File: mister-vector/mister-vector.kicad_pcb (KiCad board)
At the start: 4 copper layers, 68.6 x 106.6 mm, 132 parts, among them IC1 SN74ALVCH16841DL, IC2 74HC32D, IC3 74HC139D, IC4 SN74ALVCH16841DL, IC5 TL084, IC6 SN74ALVCH16841DL, IC7 TL084, J2 AUDIO_JACK_3.5MM_KIT, U1 VASD1-SIP

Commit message: relink refdegs
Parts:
- GPIO1: value (none) -> PINHD-2X20
- IC2: value 74HC32D -> 7432D
- IC3: value 74HC139D -> 74139D
- J1, J3: value (none) -> 618015330923
- JP1: value (none) -> JP2E
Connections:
- net +12V_OPAMP renamed /+12V_OPAMP
- net +VREF renamed /+VREF
- net -12V_OPAMP renamed /-12V_OPAMP
- net AUDIO_L renamed /AUDIO_L
- net AUDIO_R renamed /AUDIO_R
- net B+ renamed /B+
- net B1+ renamed Net-(IC5C-OUT)
- net BTN_OSD renamed /BTN_OSD
- net BTN_RESET renamed /BTN_RESET
- net BTN_USER renamed /BTN_USER
- net DAC1_B0 renamed /DAC1_B0
- net DAC1_B1 renamed /DAC1_B1
- net DAC1_B2 renamed /DAC1_B2
- net DAC1_B3 renamed /DAC1_B3
- net DAC1_B4 renamed /DAC1_B4
- net DAC1_B5 renamed /DAC1_B5
- net DAC1_G0 renamed /DAC1_G0
- net DAC1_G1 renamed /DAC1_G1
- net DAC1_G2 renamed /DAC1_G2
- net DAC1_G3 renamed /DAC1_G3
- net DAC1_G4 renamed /DAC1_G4
- net DAC1_G5 renamed /DAC1_G5
- net DAC1_HSYNC renamed /DAC1_HSYNC
- net DAC1_LAT renamed /DAC1_LAT
- net DAC1_R0 renamed /DAC1_R0
- net DAC1_R1 renamed /DAC1_R1
- net DAC1_R2 renamed /DAC1_R2
- net DAC1_R3 renamed /DAC1_R3
- net DAC1_R4 renamed /DAC1_R4
- net DAC1_R5 renamed /DAC1_R5
- net DAC1_VSYNC renamed /DAC1_VSYNC
- net DAC2_B0 renamed /DAC2_B0
- net DAC2_B1 renamed /DAC2_B1
- net DAC2_B2 renamed /DAC2_B2
- net DAC2_B3 renamed /DAC2_B3
- net DAC2_B4 renamed /DAC2_B4
- net DAC2_B5 renamed /DAC2_B5
- net DAC2_G0 renamed /DAC2_G0
- net DAC2_G1 renamed /DAC2_G1
- net DAC2_G2 renamed /DAC2_G2
- net DAC2_G3 renamed /DAC2_G3
- net DAC2_G4 renamed /DAC2_G4
- net DAC2_G5 renamed /DAC2_G5
- net DAC2_HSYNC renamed /DAC2_HSYNC
- net DAC2_LAT renamed /DAC2_LAT
- net DAC2_R0 renamed /DAC2_R0
- net DAC2_R1 renamed /DAC2_R1
- net DAC2_R2 renamed /DAC2_R2
- net DAC2_R3 renamed /DAC2_R3
- net DAC2_R4 renamed /DAC2_R4
- net DAC2_R5 renamed /DAC2_R5
- net DAC2_VSYNC renamed /DAC2_VSYNC
- net DAC3_LAT renamed /DAC3_LAT
- net DAC4_LAT renamed /DAC4_LAT
- net DAC_X renamed /DAC_X
- net DAC_Y renamed /DAC_Y
- net G+ renamed /G+
- net G1+ renamed Net-(IC5A-OUT)
- net HSYNC renamed /HSYNC
- net I1+ renamed Net-(IC5D-OUT)
- net LATCH_EN_N renamed /LATCH_EN_N
- net LED_DISK renamed /LED_DISK
- net LED_POWER renamed /LED_POWER
- net LED_USER renamed /LED_USER
- net R+ renamed /R+
- net R1+ renamed Net-(IC5B-OUT)
- net SD_CLK renamed /SD_CLK
- net SD_CMD renamed /SD_CMD
- net SD_DAT0 renamed /SD_DAT0
- net SD_DAT1 renamed /SD_DAT1
- net SD_DAT2 renamed /SD_DAT2
- net SD_DAT3 renamed /SD_DAT3
- net SPDIF renamed /SPDIF
- net VEC_X+ renamed /VEC_X+
- net VEC_X0 renamed /VEC_X0
- net VEC_X1 renamed /VEC_X1
- net VEC_X2 renamed /VEC_X2
- net VEC_X3 renamed /VEC_X3
- net VEC_X4 renamed /VEC_X4
- net VEC_X5 renamed /VEC_X5
- net VEC_X6 renamed /VEC_X6
- net VEC_X7 renamed /VEC_X7
- net VEC_X8 renamed /VEC_X8
- net VEC_X9 renamed /VEC_X9
- net VEC_Y+ renamed /VEC_Y+
- net VEC_Y0 renamed /VEC_Y0
- net VEC_Y1 renamed /VEC_Y1
- net VEC_Y2 renamed /VEC_Y2
- net VEC_Y3 renamed /VEC_Y3
- net VEC_Y4 renamed /VEC_Y4
- net VEC_Y5 renamed /VEC_Y5
- net VEC_Y6 renamed /VEC_Y6
- net VEC_Y7 renamed /VEC_Y7
- net VEC_Y8 renamed /VEC_Y8
- net VEC_Y9 renamed /VEC_Y9
- net VGA1_B renamed /VGA1_B
- net VGA1_G renamed /VGA1_G
- net VGA1_HSYNC renamed /VGA1_HSYNC
- net VGA1_R renamed /VGA1_R
- net VGA1_VSYNC renamed /VGA1_VSYNC
- net VGA2_B renamed /VGA2_B
- net VGA2_G renamed /VGA2_G
- net VGA2_HSYNC renamed /VGA2_HSYNC
- net VGA2_R renamed /VGA2_R
- net VGA2_VSYNC renamed /VGA2_VSYNC
- net VGA_B0 renamed /VGA_B0
- net VGA_B1 renamed /VGA_B1
- net VGA_B2 renamed /VGA_B2
- net VGA_B3 renamed /VGA_B3
- net VGA_B4 renamed /VGA_B4
- net VGA_B5 renamed /VGA_B5
- net VGA_G0 renamed /VGA_G0
- net VGA_G1 renamed /VGA_G1
- net VGA_G2 renamed /VGA_G2
- net VGA_G3 renamed /VGA_G3
- net VGA_G4 renamed /VGA_G4
- net VGA_G5 renamed /VGA_G5
- net VGA_R0 renamed /VGA_R0
- net VGA_R1 renamed /VGA_R1
- net VGA_R2 renamed /VGA_R2
- net VGA_R3 renamed /VGA_R3
- net VGA_R4 renamed /VGA_R4
- net VGA_R5 renamed /VGA_R5
- net VSYNC renamed /VSYNC
- IC3 pad 11: (no net) -> unconnected-(IC3B-Y1-Pad11)
- IC3 pad 12: (no net) -> unconnected-(IC3B-Y0-Pad12)
- IC3 pad 9: (no net) -> unconnected-(IC3B-Y3-Pad9)
- J1 pad 11: (no net) -> unconnected-(J1-Pad11)
- J1 pad 12: (no net) -> unconnected-(J1-Pad12)
- J1 pad 15: (no net) -> unconnected-(J1-Pad15)
- J1 pad 4: (no net) -> unconnected-(J1-Pad4)
- J1 pad 9: (no net) -> unconnected-(J1-Pad9)
- J1 pad SHELL: (no net) -> Net-(J1-SHIELD-PadSHELL)
- J1 pad SHELL1: (no net) -> Net-(J1-SHIELD-PadSHELL)
- J2 pad RSH: (no net) -> unconnected-(J2-PadRSH)
- J2 pad TSH: (no net) -> unconnected-(J2-PadTSH)
- J3 pad 11: (no net) -> unconnected-(J3-Pad11)
- J3 pad 12: (no net) -> unconnected-(J3-Pad12)
- J3 pad 15: (no net) -> unconnected-(J3-Pad15)
- J3 pad 4: (no net) -> unconnected-(J3-Pad4)
- J3 pad 9: (no net) -> unconnected-(J3-Pad9)
- J3 pad SHELL: (no net) -> Net-(J3-SHIELD-PadSHELL)
- J3 pad SHELL1: (no net) -> Net-(J3-SHIELD-PadSHELL)
- X_SIZE0 pad A: (no net) -> unconnected-(X_SIZE0-PadA)
- Y_SIZE0 pad A: (no net) -> unconnected-(Y_SIZE0-PadA)
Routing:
- added copper zone on B.Cu, net (none)
- added copper zone on F.Cu, net (none)
- added copper zone on In1.Cu, net (none)
- added copper zone on In2.Cu, net (none)
- removed copper zone on B.Cu, net GND
- removed copper zone on F.Cu, net GND
- removed copper zone on In1.Cu, net GND
- removed copper zone on In2.Cu, net GND

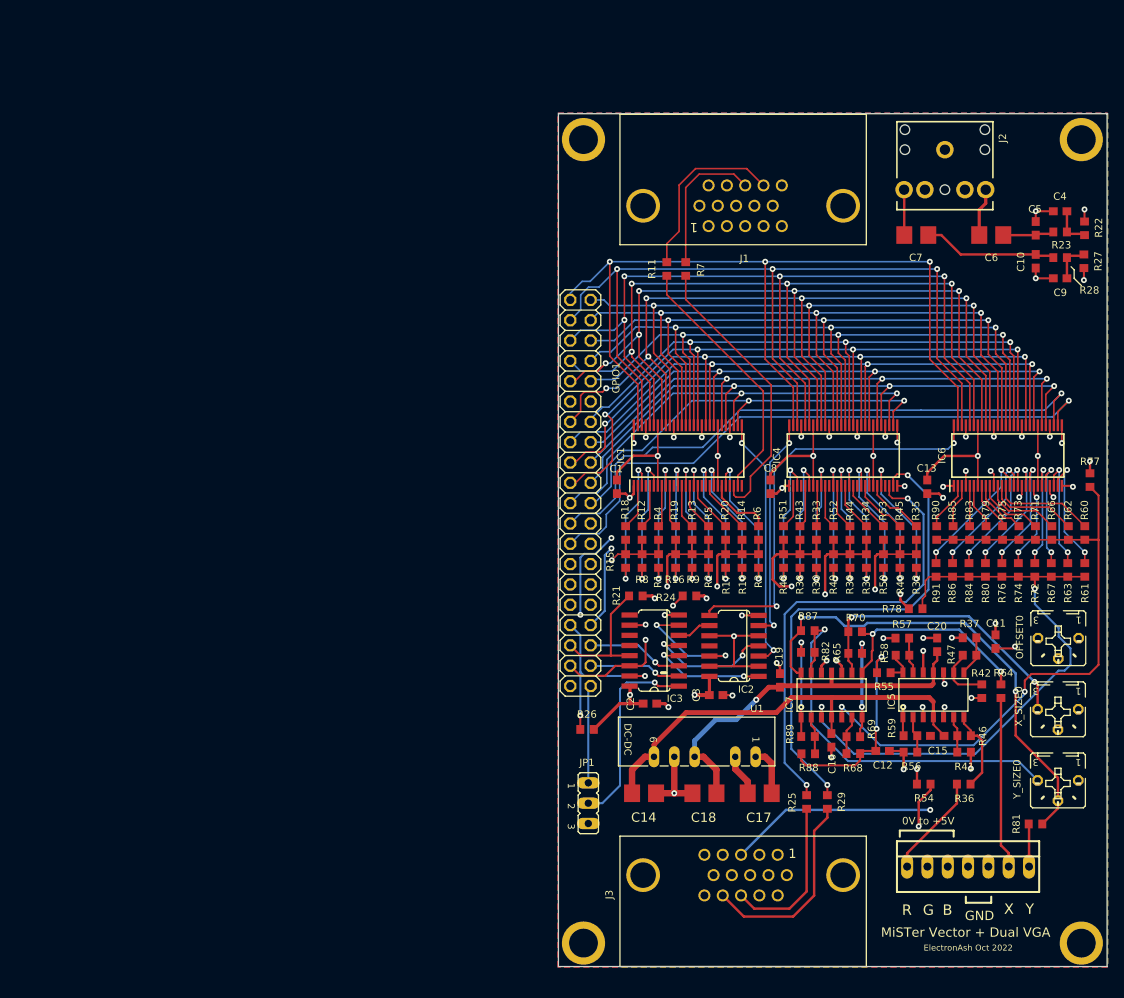
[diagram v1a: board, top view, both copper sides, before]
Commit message: reworking for r2r-dac and edge triggered buffers
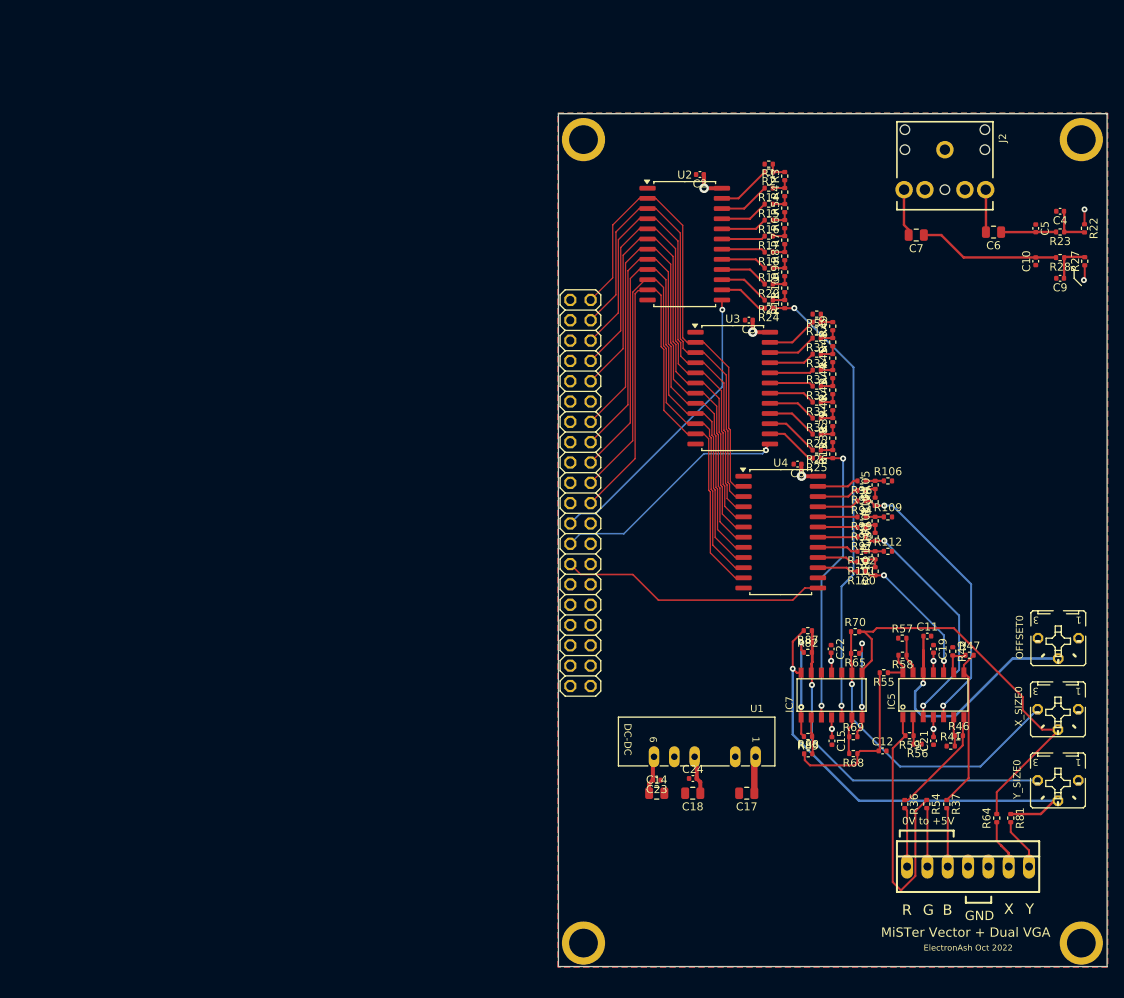
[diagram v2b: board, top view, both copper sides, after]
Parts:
- removed C1, C13: 100nF, C0603
- removed C16, C20: 0.1uF, C0603
- removed IC1, IC4, IC6: SN74ALVCH16841DL, SOP50P810X120-56N
- removed IC2: 7432D, SO14_85
- removed IC3: 74139D, SO16
- removed J1, J3: 618015330923, 618015330923
- removed JP1: JP2E, JP2_252
- removed R51, R52, R53, R75, R76: 18K, R0603
- removed R60, R61, R77, R78: 510R, R0603
- removed R62, R63: 1K1, R0603
- removed R66, R67: 2K2, R0603
- removed R71, R72: 4K3, R0603
- removed R73, R74: 9K1, R0603
- removed R79, R80: 36K, R0603
- removed R83, R84: 75K, R0603
- removed R85, R86: 150K, R0603
- removed R90, R91: 300K, R0603
- added C21: 100nF, Capacitor_SMD:C_0402_1005Metric, F.Cu at (161.1, 130.1)
- added C22: 100nF, Capacitor_SMD:C_0402_1005Metric, F.Cu at (148.3, 118.6)
- added C23: 100nF, Capacitor_SMD:C_0402_1005Metric, F.Cu at (126.5, 135.0)
- added C24: 100nF, Capacitor_SMD:C_0402_1005Metric, F.Cu at (131.0, 134.8)
- added R100: 2k, Resistor_SMD:R_0402_1005Metric, F.Cu at (152.1, 108.9)
- added R101: 2k, Resistor_SMD:R_0402_1005Metric, F.Cu at (152.1, 107.7)
- added R102: 2k, Resistor_SMD:R_0402_1005Metric, F.Cu at (152.1, 106.4)
- added R104: 1k, Resistor_SMD:R_0402_1005Metric, F.Cu at (153.8, 100.2)
- added R105: 1k, Resistor_SMD:R_0402_1005Metric, F.Cu at (153.8, 98.1)
- added R106: 2k, Resistor_SMD:R_0402_1005Metric, F.Cu at (155.4, 97.6)
- added R107: 1k, Resistor_SMD:R_0402_1005Metric, F.Cu at (153.8, 104.6)
- added R108: 1k, Resistor_SMD:R_0402_1005Metric, F.Cu at (153.8, 102.6)
- added R109: 2k, Resistor_SMD:R_0402_1005Metric, F.Cu at (155.4, 102.1)
- added R110: 1k, Resistor_SMD:R_0402_1005Metric, F.Cu at (153.8, 108.9)
- added R111: 1k, Resistor_SMD:R_0402_1005Metric, F.Cu at (153.8, 106.9)
- added R112: 2k, Resistor_SMD:R_0402_1005Metric, F.Cu at (155.4, 106.4)
- added R94: 2k, Resistor_SMD:R_0402_1005Metric, F.Cu at (152.1, 100.1)
- added R95: 2k, Resistor_SMD:R_0402_1005Metric, F.Cu at (152.1, 98.8)
- added R96: 2k, Resistor_SMD:R_0402_1005Metric, F.Cu at (152.1, 97.6)
- added R97: 2k, Resistor_SMD:R_0402_1005Metric, F.Cu at (152.1, 104.6)
- added R98: 2k, Resistor_SMD:R_0402_1005Metric, F.Cu at (152.1, 103.4)
- added R99: 2k, Resistor_SMD:R_0402_1005Metric, F.Cu at (152.1, 102.1)
- added U2: SN74LVC821ADGVR, Package_SO:SOIC-24W_7.5x15.4mm_P1.27mm, F.Cu at (130.0, 68.0)
- added U3: SN74LVC821ADGVR, Package_SO:SOIC-24W_7.5x15.4mm_P1.27mm, F.Cu at (136.0, 86.0)
- added U4: SN74LVC821ADGVR, Package_SO:SOIC-24W_7.5x15.4mm_P1.27mm, F.Cu at (142.0, 104.0)
- C10, C11, C12, C2, C3, C4, C5, C8, C9: footprint C0603 -> Capacitor_SMD:C_0402_1005Metric
- C14, C17, C18: footprint CT3528 -> Capacitor_SMD:C_0805_2012Metric
- C15, C19: value 0.1uF -> 100nF; footprint C0603 -> Capacitor_SMD:C_0402_1005Metric
- C6, C7: value 4.7uF -> 4.7uF BP; footprint CT3528 -> Capacitor_SMD:C_0805_2012Metric
- R1, R2, R30, R31, R32: value 510R -> 2k; footprint R0603 -> Resistor_SMD:R_0402_1005Metric
- R10, R38, R39, R40, R8, R9: value 2K2 -> 1k; footprint R0603 -> Resistor_SMD:R_0402_1005Metric
- R11, R7: value 100R -> 1k; footprint R0603 -> Resistor_SMD:R_0402_1005Metric
- R12, R14: value 4K3 -> 2k; footprint R0603 -> Resistor_SMD:R_0402_1005Metric
- R13, R43, R44, R45: value 4K3 -> 1k; footprint R0603 -> Resistor_SMD:R_0402_1005Metric
- R15, R16, R17, R50: value 9K1 -> 2k; footprint R0603 -> Resistor_SMD:R_0402_1005Metric
- R18, R19, R20: value 18K -> 2k; footprint R0603 -> Resistor_SMD:R_0402_1005Metric
- R21, R24, R26: value 10K -> 2k; footprint R0603 -> Resistor_SMD:R_0402_1005Metric
- R22, R23, R27, R28, R36, R37, R41, R42, R46, R47, R54, R55, R56, R57, R58, R59, R64, R65, R68, R69, R70, R81, R82, R87, R88, R89: footprint R0603 -> Resistor_SMD:R_0402_1005Metric
- R25, R29: value 100R -> 2k; footprint R0603 -> Resistor_SMD:R_0402_1005Metric
- R3: value 510R -> 1k; footprint R0603 -> Resistor_SMD:R_0402_1005Metric
- R33, R34, R35: value 1K1 -> 2k; footprint R0603 -> Resistor_SMD:R_0402_1005Metric
- R4, R5, R6: value 1K1 -> 1k; footprint R0603 -> Resistor_SMD:R_0402_1005Metric
- R48, R49: value 9K1 -> 1k; footprint R0603 -> Resistor_SMD:R_0402_1005Metric
- moved C2 66.4 mm to (131.9, 59.3), turned to 180 degrees
- moved R1 51.5 mm to (140.5, 58.0), turned to 180 degrees
- moved R2 49.2 mm to (140.5, 59.0), turned to 180 degrees
- moved R3 48.2 mm to (142.5, 59.5)
- moved R15 48.1 mm to (140.5, 63.0), turned to 180 degrees
- moved C3 47.0 mm to (138.0, 77.5), turned to 180 degrees
- moved R29 46.0 mm to (146.5, 91.8), turned to 180 degrees
- moved R4 45.4 mm to (142.5, 61.5), turned to 90 degrees
- moved R26 45.2 mm to (146.5, 93.8)
- moved R16 44.2 mm to (140.5, 65.0), turned to 180 degrees
- moved R14 43.2 mm to (140.5, 61.0), turned to 180 degrees
- moved R25 43.0 mm to (146.5, 94.8), turned to 180 degrees
- moved R8 42.1 mm to (142.5, 69.5)
- moved R5 41.7 mm to (142.5, 63.5), turned to 90 degrees
- moved R17 41.0 mm to (140.5, 67.0), turned to 180 degrees
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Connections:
- net /B+ renamed /B
- net /G+ renamed /G
- net /R+ renamed /R
- net /VEC_X+ renamed /VEC_X
- net /VEC_Y+ renamed /VEC_Y
- C10 pad 1: Net-(C10-Pad1) -> GND
- C10 pad 2: GND -> Net-(C10-Pad2)
- C15 pad 1: /+12V_OPAMP -> +12V
- C19 pad 2: /-12V_OPAMP -> -12V
- C2 pad 1: +3V3 -> +3.3V
- C3 pad 1: +3V3 -> +3.3V
- C8 pad 1: +3V3 -> +3.3V
- C9 pad 1: GND -> Net-(C9-Pad1)
- C9 pad 2: Net-(C9-Pad2) -> GND
- GPIO1 pad 14: /SD_CLK -> /CLK_RGB
- GPIO1 pad 16: /SD_DAT0 -> /CLK_Y
- GPIO1 pad 18: /SD_DAT1 -> /CLK_X
- GPIO1 pad 19: /VSYNC -> /D9
- GPIO1 pad 20: /HSYNC -> unconnected-(GPIO1-Pad20)
- GPIO1 pad 21: /VGA_B5 -> /D8
- GPIO1 pad 22: /VGA_B0 -> unconnected-(GPIO1-Pad22)
- GPIO1 pad 23: /VGA_B4 -> /D7
- GPIO1 pad 24: /VGA_B1 -> unconnected-(GPIO1-Pad24)
- GPIO1 pad 25: /VGA_B3 -> /D6
- GPIO1 pad 26: /VGA_B2 -> unconnected-(GPIO1-Pad26)
- GPIO1 pad 27: /VGA_G5 -> /D5
- GPIO1 pad 28: /VGA_R5 -> unconnected-(GPIO1-Pad28)
- GPIO1 pad 29: +3V3 -> +3.3V
- GPIO1 pad 31: /VGA_G4 -> /D4
- GPIO1 pad 32: /VGA_R4 -> unconnected-(GPIO1-Pad32)
- GPIO1 pad 33: /VGA_G3 -> /D3
- GPIO1 pad 34: /VGA_R3 -> unconnected-(GPIO1-Pad34)
- GPIO1 pad 35: /VGA_G2 -> /D2
- GPIO1 pad 36: /VGA_R2 -> unconnected-(GPIO1-Pad36)
- GPIO1 pad 37: /VGA_G1 -> /D1
- GPIO1 pad 38: /VGA_R1 -> unconnected-(GPIO1-Pad38)
- GPIO1 pad 39: /VGA_G0 -> /D0
- GPIO1 pad 40: /VGA_R0 -> unconnected-(GPIO1-Pad40)
- IC5 pad 10: /VGA2_B -> /DAC_B
- IC5 pad 11: /-12V_OPAMP -> -12V
- IC5 pad 3: /VGA2_G -> /DAC_G
- IC5 pad 4: /+12V_OPAMP -> +12V
- IC5 pad 5: /VGA2_R -> /DAC_R
- IC7 pad 11: /-12V_OPAMP -> -12V
- IC7 pad 4: /+12V_OPAMP -> +12V
- J2 pad RING: Net-(C6-Pad-) -> Net-(C6-Pad2)
- J2 pad TIP: Net-(C7-Pad-) -> Net-(C7-Pad2)
- OFFSET0 pad E: +3V3 -> +3.3V
- R1 pad 1: /DAC1_R5 -> Net-(R1-Pad1)
- R1 pad 2: /VGA1_R -> GND
- R10 pad 1: /DAC1_B3 -> Net-(R10-Pad1)
- R10 pad 2: /VGA1_B -> Net-(R10-Pad2)
- R11 pad 1: /DAC1_VSYNC -> /DAC_X
- R11 pad 2: /VGA1_VSYNC -> Net-(R10-Pad1)
- R12 pad 1: /DAC1_R2 -> Net-(R12-Pad1)
- R12 pad 2: /VGA1_R -> /R2R_DAC_Y/D0
- R13 pad 1: /DAC1_G2 -> /DAC_Y
- R13 pad 2: /VGA1_G -> Net-(R13-Pad2)
- R14 pad 1: /DAC1_B2 -> Net-(R14-Pad1)
- R14 pad 2: /VGA1_B -> /R2R_DAC_X/D1
- R15 pad 1: /DAC1_R1 -> Net-(R15-Pad1)
- R15 pad 2: /VGA1_R -> /R2R_DAC_X/D2
- R16 pad 1: /DAC1_G1 -> Net-(R16-Pad1)
- R16 pad 2: /VGA1_G -> /R2R_DAC_X/D3
- R17 pad 1: /DAC1_B1 -> Net-(R17-Pad1)
- R17 pad 2: /VGA1_B -> /R2R_DAC_X/D4
- R18 pad 1: /DAC1_R0 -> Net-(R18-Pad1)
- R18 pad 2: /VGA1_R -> /R2R_DAC_X/D5
- R19 pad 1: /DAC1_G0 -> Net-(R19-Pad1)
- R19 pad 2: /VGA1_G -> /R2R_DAC_X/D6
- R2 pad 1: /DAC1_G5 -> Net-(R1-Pad1)
- R2 pad 2: /VGA1_G -> /R2R_DAC_X/D0
- R20 pad 1: /DAC1_B0 -> Net-(R10-Pad2)
- R20 pad 2: /VGA1_B -> /R2R_DAC_X/D7
- R21 pad 1: +3V3 -> Net-(R10-Pad1)
- R21 pad 2: /SD_DAT3 -> /R2R_DAC_X/D8
- R24 pad 1: +3V3 -> /DAC_X
- R24 pad 2: /SD_DAT2 -> /R2R_DAC_X/D9
- R25 pad 1: /DAC2_HSYNC -> /DAC_Y
- R25 pad 2: /VGA2_HSYNC -> /R2R_DAC_Y/D9
- R26 pad 1: +3V3 -> Net-(R13-Pad2)
- R26 pad 2: /SD_CMD -> /R2R_DAC_Y/D8
- R27 pad 2: Net-(C9-Pad2) -> Net-(C9-Pad1)
- R28 pad 1: Net-(C9-Pad2) -> Net-(C9-Pad1)
- R28 pad 2: Net-(C10-Pad1) -> Net-(C10-Pad2)
- R29 pad 1: /DAC2_VSYNC -> Net-(R29-Pad1)
- R29 pad 2: /VGA2_VSYNC -> /R2R_DAC_Y/D7
- R3 pad 1: /DAC1_B5 -> Net-(R14-Pad1)
- R3 pad 2: /VGA1_B -> Net-(R1-Pad1)
- R30 pad 1: /DAC2_R5 -> Net-(R30-Pad1)
- R30 pad 2: /VGA2_R -> /R2R_DAC_Y/D6
- R31 pad 1: /DAC2_G5 -> Net-(R31-Pad1)
- R31 pad 2: /VGA2_G -> /R2R_DAC_Y/D5
- R32 pad 1: /DAC2_B5 -> Net-(R32-Pad1)
- R32 pad 2: /VGA2_B -> /R2R_DAC_Y/D4
- R33 pad 1: /DAC2_R4 -> Net-(R33-Pad1)
- R33 pad 2: /VGA2_R -> /R2R_DAC_Y/D3
- R34 pad 1: /DAC2_G4 -> Net-(R34-Pad1)
- R34 pad 2: /VGA2_G -> /R2R_DAC_Y/D2
- R35 pad 1: /DAC2_B4 -> Net-(R35-Pad1)
- R35 pad 2: /VGA2_B -> /R2R_DAC_Y/D1
- R38 pad 1: /DAC2_R3 -> Net-(R13-Pad2)
- R38 pad 2: /VGA2_R -> Net-(R29-Pad1)
- R39 pad 1: /DAC2_G3 -> Net-(R29-Pad1)
- R39 pad 2: /VGA2_G -> Net-(R30-Pad1)
- R4 pad 1: /DAC1_R4 -> Net-(R15-Pad1)
- R4 pad 2: /VGA1_R -> Net-(R14-Pad1)
- R40 pad 1: /DAC2_B3 -> Net-(R30-Pad1)
- R40 pad 2: /VGA2_B -> Net-(R31-Pad1)
- R43 pad 1: /DAC2_R2 -> Net-(R31-Pad1)
- R43 pad 2: /VGA2_R -> Net-(R32-Pad1)
- R44 pad 1: /DAC2_G2 -> Net-(R32-Pad1)
- R44 pad 2: /VGA2_G -> Net-(R33-Pad1)
- R45 pad 1: /DAC2_B2 -> Net-(R33-Pad1)
- R45 pad 2: /VGA2_B -> Net-(R34-Pad1)
- R48 pad 1: /DAC2_R1 -> Net-(R34-Pad1)
- R48 pad 2: /VGA2_R -> Net-(R35-Pad1)
- R49 pad 1: /DAC2_G1 -> Net-(R35-Pad1)
- R49 pad 2: /VGA2_G -> Net-(R12-Pad1)
- R5 pad 1: /DAC1_G4 -> Net-(R16-Pad1)
- R5 pad 2: /VGA1_G -> Net-(R15-Pad1)
- R50 pad 1: /DAC2_B1 -> Net-(R12-Pad1)
- R50 pad 2: /VGA2_B -> GND
- R6 pad 1: /DAC1_B4 -> Net-(R17-Pad1)
- R6 pad 2: /VGA1_B -> Net-(R16-Pad1)
- R7 pad 1: /DAC1_HSYNC -> Net-(R18-Pad1)
- R7 pad 2: /VGA1_HSYNC -> Net-(R17-Pad1)
- R8 pad 1: /DAC1_R3 -> Net-(R19-Pad1)
- R8 pad 2: /VGA1_R -> Net-(R18-Pad1)
- R9 pad 1: /DAC1_G3 -> Net-(R10-Pad2)
- R9 pad 2: /VGA1_G -> Net-(R19-Pad1)
- U1 pad 4: /-12V_OPAMP -> -12V
- U1 pad 6: /+12V_OPAMP -> +12V
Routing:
- net +3V3: track 231.4 -> 0.00 mm, vias 10 -> 0
- net +3.3V: track 0.00 -> 122.5 mm, vias 0 -> 3
- net /VGA_R0: track 113.1 -> 0.00 mm, vias 3 -> 0
- net /VGA_R1: track 112.0 -> 0.00 mm, vias 3 -> 0
- net /VGA_R2: track 107.6 -> 0.00 mm, vias 4 -> 0
- net /VGA_R3: track 105.8 -> 0.00 mm, vias 4 -> 0
- net /VGA_R5: track 104.9 -> 0.00 mm, vias 5 -> 0
- net /VGA_R4: track 104.9 -> 0.00 mm, vias 5 -> 0
- net /VGA_B0: track 96.3 -> 0.00 mm, vias 4 -> 0
- net /VGA_G0: track 95.6 -> 0.00 mm, vias 3 -> 0
- net /VGA_G1: track 93.9 -> 0.00 mm, vias 3 -> 0
- net /VGA_G2: track 92.3 -> 0.00 mm, vias 3 -> 0
- net /VGA_G3: track 90.6 -> 0.00 mm, vias 3 -> 0
- net /VGA_B1: track 90.0 -> 0.00 mm, vias 4 -> 0
- net /LATCH_EN_N: track 89.2 -> 0.00 mm, vias 4 -> 0
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- added copper zone on B.Cu, net GND
- added copper zone on F.Cu, net GND
- added copper zone on In1.Cu, net GND
- added copper zone on In2.Cu, net GND
- removed copper zone on B.Cu, net (none)
- removed copper zone on F.Cu, net (none)
- removed copper zone on In1.Cu, net (none)
- removed copper zone on In2.Cu, net (none)

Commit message: update pcb screenshot
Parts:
- removed GPIO1: PINHD-2X20, 2X20
- removed IC5, IC7: TL084, SOIC-14
- removed J2: AUDIO_JACK_3.5MM_KIT, AUDIO-JACK-KIT
- removed OFFSET0, X_SIZE0, Y_SIZE0: 20K, B25P
- removed R100, R102, R106, R109, R112, R31, R32, R33, R94, R95, R96: 2k, Resistor_SMD:R_0402_1005Metric
- removed R104, R105, R107, R108, R110, R111, R43: 1k, Resistor_SMD:R_0402_1005Metric
- removed R41, R42: 10K, Resistor_SMD:R_0402_1005Metric
- removed U$1, U$2, U$3, U$4: PLATED_HOLE3.6MM, PLATED_HOLE_3.6MM
- removed VEC_OUT1: 22-23-2071, 22-23-2071
- added C1: 100nF, Capacitor_SMD:C_0402_1005Metric, F.Cu at (80.1, 95.1)
- added C13: 100nF, Capacitor_SMD:C_0402_1005Metric, F.Cu at (99.4, 61.8)
- added C16: 1uF, Capacitor_SMD:C_0603_1608Metric, F.Cu at (73.6, 71.1)
- added C20: 100nF, Capacitor_SMD:C_0402_1005Metric, F.Cu at (83.8, 69.6)
- added C25: 0.1pF, Capacitor_SMD:C_0402_1005Metric, F.Cu at (73.7, 125.7)
- added C26: 0.1pF, Capacitor_SMD:C_0402_1005Metric, F.Cu at (73.7, 121.8)
- added C27: 0.1pF, Capacitor_SMD:C_0402_1005Metric, F.Cu at (73.7, 129.7)
- added C40: 20nF, Capacitor_SMD:C_0402_1005Metric, F.Cu at (91.0, 99.9)
- added C41: 20nF, Capacitor_SMD:C_0402_1005Metric, F.Cu at (98.7, 99.9)
- added C47: 1uF, Capacitor_SMD:C_0603_1608Metric, F.Cu at (149.2, 105.0)
- added G***: LOGO, LOGO, F.Cu at (53.6, 56.7)
- added H1: MountingHole_Pad, MountingHole:MountingHole_3mm_Pad_Via, F.Cu at (159.4, 154.9)
- added H2: MountingHole_Pad, MountingHole:MountingHole_3mm_Pad_Via, F.Cu at (58.9, 92.7)
- added H3: MountingHole_Pad, MountingHole:MountingHole_3mm_Pad_Via, F.Cu at (159.4, 92.7)
- added H4: MountingHole_Pad, MountingHole:MountingHole_3mm_Pad_Via, F.Cu at (58.9, 154.9)
- added H5: FAN1, MountingHole:MountingHole_3mm, F.Cu at (66.4, 116.6)
- added H6: FAN2, MountingHole:MountingHole_3mm, F.Cu at (66.4, 124.2)
- added H7: FAN3, MountingHole:MountingHole_3mm, F.Cu at (66.4, 131.7)
- added H8: FAN4, MountingHole:MountingHole_3mm, F.Cu at (66.4, 139.2)
- added J10: DC-005-2.5A-2.0 C319099, Connector_BarrelJack:BarrelJack_Horizontal, F.Cu at (148.6, 145.5)
- added J100: FAN, Connector_PinHeader_2.54mm:PinHeader_1x03_P2.54mm_Vertical, F.Cu at (133.1, 140.9)
- added J7: PINHD-2X20, Connector_PinSocket_2.54mm:PinSocket_2x20_P2.54mm_Vertical, B.Cu at (91.1, 93.6)
- added J8: Jamma_con, Jamma:JAMMA-56, F.Cu at (158.9, 43.9)
- added R51: 100k, Resistor_SMD:R_0402_1005Metric, F.Cu at (85.1, 54.5)
- added R52: 100k, Resistor_SMD:R_0402_1005Metric, F.Cu at (85.1, 55.6)
- added R53: 100k, Resistor_SMD:R_0402_1005Metric, F.Cu at (85.1, 56.7)
- added R60: 100k, Resistor_SMD:R_0402_1005Metric, F.Cu at (73.3, 55.4)
- added R61: 75R, Resistor_SMD:R_0402_1005Metric, F.Cu at (74.1, 77.7)
- added R62: 75R, Resistor_SMD:R_0402_1005Metric, F.Cu at (73.5, 79.4)
- added R63: 10K, Resistor_SMD:R_0402_1005Metric, F.Cu at (85.7, 80.3)
- added R66: 75R, Resistor_SMD:R_0402_1005Metric, F.Cu at (73.6, 86.8)
- added R67: 75R, Resistor_SMD:R_0402_1005Metric, F.Cu at (84.2, 86.1)
- added R71: 75R, Resistor_SMD:R_0402_1005Metric, F.Cu at (85.1, 65.6)
- added R72: 75R, Resistor_SMD:R_0402_1005Metric, F.Cu at (84.9, 74.0)
- added R73: 75R, Resistor_SMD:R_0402_1005Metric, F.Cu at (74.1, 64.9)
- added R74: 10K, Resistor_SMD:R_0402_1005Metric, F.Cu at (85.1, 67.7)
- added R75: 10K, Resistor_SMD:R_0402_1005Metric, F.Cu at (73.4, 66.6)
- added R76: 10K, Resistor_SMD:R_0402_1005Metric, F.Cu at (85.3, 72.2)
- added R77: 4K7, Resistor_SMD:R_0402_1005Metric, F.Cu at (83.8, 66.6)
- added R78: 4K7, Resistor_SMD:R_0402_1005Metric, F.Cu at (74.6, 66.6)
- added R79: 4K7, Resistor_SMD:R_0402_1005Metric, F.Cu at (83.7, 72.9)
- added R80: 75R, Resistor_SMD:R_0402_1005Metric, F.Cu at (77.2, 75.3)
- added R83: 100k, Resistor_SMD:R_0402_1005Metric, F.Cu at (73.3, 56.5)
- added R84: 100k, Resistor_SMD:R_0402_1005Metric, F.Cu at (73.3, 57.6)
- added R85: 100k, Resistor_SMD:R_0402_1005Metric, F.Cu at (73.3, 58.7)
- added R86: 100k, Resistor_SMD:R_0402_1005Metric, F.Cu at (73.3, 59.8)
- added R90: 100k, Resistor_SMD:R_0402_1005Metric, F.Cu at (96.9, 57.7)
- added R91: 100k, Resistor_SMD:R_0402_1005Metric, F.Cu at (96.9, 58.8)
- added R92: 100k, Resistor_SMD:R_0402_1005Metric, F.Cu at (96.9, 59.9)
- added U10: TXB0106PWR, TXB0106PWR:SOP65P640X120-16N, F.Cu at (101.5, 57.2)
- added U12: LM4871MX_NOPB, LM4871MX_NOPB:SOIC127P599X175-8N, F.Cu at (154.3, 106.4)
- added U13: TL084HIDR, Package_SO:SOIC-14_3.9x8.7mm_P1.27mm, F.Cu at (79.2, 82.5)
- added U14: TL084HIDR, Package_SO:SOIC-14_3.9x8.7mm_P1.27mm, F.Cu at (79.2, 69.7)
- added U5: TXB0106PWR, TXB0106PWR:SOP65P640X120-16N, F.Cu at (89.8, 57.2)
- added U6: TXB0106PWR, TXB0106PWR:SOP65P640X120-16N, F.Cu at (77.8, 57.3)
- added U7: SN74LVC821ADGVR, Package_SO:SOIC-24W_7.5x15.4mm_P1.27mm, F.Cu at (107.3, 74.1)
- added U8: SN74LVC821ADGVR, Package_SO:SOIC-24W_7.5x15.4mm_P1.27mm, F.Cu at (150.8, 72.1)
- added U9: SN74LVC821ADGVR, Package_SO:SOIC-24W_7.5x15.4mm_P1.27mm, F.Cu at (133.1, 74.1)
- added VR1: VREF, 3362P_1_203LF:TRIM_3362P-1-203LF, F.Cu at (67.9, 71.3)
- added VR2: X_SIZE, 3362P_1_203LF:TRIM_3362P-1-203LF, F.Cu at (67.9, 79.8)
- added VR3: Y_SIZE, 3362P_1_203LF:TRIM_3362P-1-203LF, F.Cu at (67.9, 88.2)
- added VR4: 50k, PTV09A-4020U-A503:PTV09A4020FB103, F.Cu at (139.4, 107.2)
- C10, C4, C9: value 10nF -> 100nF
- C11, C12: value 1.0uF -> 100nF
- C14: value 4.7uF -> 0.1pF; footprint Capacitor_SMD:C_0805_2012Metric -> Capacitor_SMD:C_0402_1005Metric
- C15: value 100nF -> 0.1pF
- C17: value 4.7uF -> 1uF; footprint Capacitor_SMD:C_0805_2012Metric -> Capacitor_SMD:C_0603_1608Metric
- C18: value 4.7uF -> 100nF; footprint Capacitor_SMD:C_0805_2012Metric -> Capacitor_SMD:C_0402_1005Metric
- C2, C3: value 100nF -> 4.7uF; footprint Capacitor_SMD:C_0402_1005Metric -> Capacitor_SMD:C_0805_2012Metric
- C5: value 10nF -> 4.7uF; footprint Capacitor_SMD:C_0402_1005Metric -> Capacitor_SMD:C_0805_2012Metric
- C6, C7: value 4.7uF BP -> 100nF; footprint Capacitor_SMD:C_0805_2012Metric -> Capacitor_SMD:C_0402_1005Metric
- R1, R12, R14, R15, R16, R17, R18, R19, R2, R20, R21, R24, R25, R26, R29, R30, R34, R35: value 2k -> 100k 0.1%
- R10, R11, R13, R3, R38, R39, R4, R40, R44, R5, R6, R7, R8, R9: value 1k -> 100k 0.1%
- R101, R99: value 2k -> 20k
- R22, R23, R27, R28: value 510R -> 100k 0.1%
- R36, R37: value 75R -> 100k 0.1%
- R45, R48, R49: value 1k -> 100k
- R46, R47, R59: value 4K7 -> 100k
- R50: value 2k -> 100k
- R54, R55: value 75R -> 100k
- R56, R87, R88, R89: value 10K -> 100k
- R57: value 10K -> 0
- R58: value 4K7 -> 0
- R64, R65, R81: value 75R -> 10K
- R82: value 75R -> 4K7
- R97, R98: value 2k -> 475R
- U1: value VASD1-SIP -> RD-0512D
- U2, U3: value SN74LVC821ADGVR -> 4816P-R2R-503LF; footprint Package_SO:SOIC-24W_7.5x15.4mm_P1.27mm -> Package_SO:SOIC-16W_5.3x10.2mm_P1.27mm
- U4: value SN74LVC821ADGVR -> TXB0106PWR; footprint Package_SO:SOIC-24W_7.5x15.4mm_P1.27mm -> TXB0106PWR:SOP65P640X120-16N
- moved R46 126.7 mm to (61.4, 55.6), turned to 180 degrees
- moved R47 121.6 mm to (61.4, 56.7), turned to 180 degrees
- moved R81 118.0 mm to (73.4, 73.1), turned to 90 degrees
- moved R59 113.3 mm to (73.3, 54.3)
- moved R54 109.9 mm to (85.1, 57.8), turned to 180 degrees
- moved C4 106.0 mm to (75.6, 95.1)
- moved C21 105.7 mm to (74.6, 69.3), turned to -90 degrees
- moved C6 105.3 mm to (64.4, 51.9), turned to 90 degrees
- moved C12 105.2 mm to (75.7, 61.9), turned to 180 degrees
- moved R64 104.1 mm to (83.9, 79.8), turned to 90 degrees
- moved C5 103.0 mm to (75.6, 96.9), turned to 0 degrees
- moved R56 102.2 mm to (85.1, 60.0)
- moved C10 99.8 mm to (75.8, 51.9)
- moved R55 93.8 mm to (85.1, 58.9)
- moved C19 93.5 mm to (74.6, 83.0), turned to 90 degrees
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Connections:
- C10 pad 1: GND -> +5V
- C10 pad 2: Net-(C10-Pad2) -> GND
- C11 pad 1: Net-(IC5D-+IN) -> +5V
- C12 pad 1: /+VREF -> +3.3V
- C14 pad 1: +12V -> GND
- C14 pad 2: GND -> /Vector Amplifiers/DAC_B
- C15 pad 1: +12V -> GND
- C15 pad 2: GND -> /Vector Amplifiers/DAC_G
- C17 pad 1: +5V -> /Vector Amplifiers/+VREF
- C18 pad 1: -12V -> GND
- C18 pad 2: GND -> +12V
- C2 pad 1: +3.3V -> +12V
- C21 pad 2: +12V -> -12V
- C22 pad 1: GND -> +3.3V
- C22 pad 2: -12V -> GND
- C23 pad 1: GND -> +3.3V
- C23 pad 2: +12V -> GND
- C24 pad 1: GND -> +3.3V
- C24 pad 2: -12V -> GND
- C3 pad 1: +3.3V -> +5V
- C4 pad 1: Net-(C4-Pad1) -> GND
- C4 pad 2: GND -> -12V
- C5 pad 1: GND -> -12V
- C5 pad 2: Net-(C5-Pad2) -> GND
- C6 pad 1: Net-(C5-Pad2) -> +5V
- C6 pad 2: Net-(C6-Pad2) -> GND
- C7 pad 1: Net-(C10-Pad2) -> +5V
- C7 pad 2: Net-(C7-Pad2) -> GND
- C9 pad 1: Net-(C9-Pad1) -> +3.3V
- R1 pad 1: Net-(R1-Pad1) -> /Vector Amplifiers/DAC_B
- R1 pad 2: GND -> /Vector DACs/R2R_DAC_B/D2
- R10 pad 1: Net-(R10-Pad1) -> /Vector Amplifiers/DAC_G
- R101 pad 1: Net-(R101-Pad1) -> /JAMMA_SPEAKER+
- R101 pad 2: /R2R_DAC_B/D1 -> Net-(U12--IN)
- R11 pad 1: /DAC_X -> /Vector Amplifiers/DAC_G
- R11 pad 2: Net-(R10-Pad1) -> Net-(R10-Pad2)
- R12 pad 1: Net-(R12-Pad1) -> Net-(R10-Pad2)
- R12 pad 2: /R2R_DAC_Y/D0 -> /Vector DACs/R2R_DAC_G/D1
- R13 pad 1: /DAC_Y -> Net-(R10-Pad2)
- R14 pad 1: Net-(R14-Pad1) -> Net-(R10-Pad2)
- R14 pad 2: /R2R_DAC_X/D1 -> Net-(R13-Pad2)
- R15 pad 1: Net-(R15-Pad1) -> Net-(R13-Pad2)
- R15 pad 2: /R2R_DAC_X/D2 -> /Vector DACs/R2R_DAC_G/D0
- R16 pad 1: Net-(R16-Pad1) -> Net-(R13-Pad2)
- R16 pad 2: /R2R_DAC_X/D3 -> GND
- R17 pad 1: Net-(R17-Pad1) -> /Vector Amplifiers/DAC_R
- R17 pad 2: /R2R_DAC_X/D4 -> /Vector DACs/R2R_DAC_R/D2
- R18 pad 1: Net-(R18-Pad1) -> /Vector Amplifiers/DAC_R
- R18 pad 2: /R2R_DAC_X/D5 -> Net-(R18-Pad2)
- R19 pad 1: Net-(R19-Pad1) -> /Vector Amplifiers/DAC_R
- R19 pad 2: /R2R_DAC_X/D6 -> Net-(R18-Pad2)
- R2 pad 1: Net-(R1-Pad1) -> /Vector Amplifiers/DAC_B
- R2 pad 2: /R2R_DAC_X/D0 -> Net-(R2-Pad2)
- R20 pad 1: Net-(R10-Pad2) -> Net-(R18-Pad2)
- R20 pad 2: /R2R_DAC_X/D7 -> /Vector DACs/R2R_DAC_R/D1
- R21 pad 1: Net-(R10-Pad1) -> Net-(R18-Pad2)
- R21 pad 2: /R2R_DAC_X/D8 -> Net-(R21-Pad2)
- R22 pad 1: /AUDIO_R -> Net-(R18-Pad2)
- R22 pad 2: Net-(C4-Pad1) -> Net-(R21-Pad2)
- R23 pad 1: Net-(C4-Pad1) -> Net-(R21-Pad2)
- R23 pad 2: Net-(C5-Pad2) -> /Vector DACs/R2R_DAC_R/D0
- R24 pad 1: /DAC_X -> Net-(R21-Pad2)
- R24 pad 2: /R2R_DAC_X/D9 -> GND
- R25 pad 1: /DAC_Y -> Net-(R25-Pad1)
- R25 pad 2: /R2R_DAC_Y/D9 -> Net-(R25-Pad2)
- R26 pad 1: Net-(R13-Pad2) -> Net-(R25-Pad1)
- R26 pad 2: /R2R_DAC_Y/D8 -> Net-(R25-Pad2)
- R27 pad 1: /AUDIO_L -> Net-(R25-Pad2)
- R27 pad 2: Net-(C9-Pad1) -> /Vector DACs/R2R_DAC_X/D1
- R28 pad 1: Net-(C9-Pad1) -> Net-(R25-Pad2)
- R28 pad 2: Net-(C10-Pad2) -> Net-(R28-Pad2)
- R29 pad 1: Net-(R29-Pad1) -> Net-(R25-Pad2)
- R29 pad 2: /R2R_DAC_Y/D7 -> Net-(R28-Pad2)
- R3 pad 1: Net-(R14-Pad1) -> /Vector Amplifiers/DAC_B
- R3 pad 2: Net-(R1-Pad1) -> Net-(R2-Pad2)
- R30 pad 1: Net-(R30-Pad1) -> Net-(R28-Pad2)
- R30 pad 2: /R2R_DAC_Y/D6 -> /Vector DACs/R2R_DAC_X/D0
- R34 pad 1: Net-(R34-Pad1) -> Net-(R28-Pad2)
- R34 pad 2: /R2R_DAC_Y/D2 -> GND
- R35 pad 2: /R2R_DAC_Y/D1 -> Net-(R35-Pad2)
- R36 pad 1: Net-(IC5B-OUT) -> Net-(R35-Pad1)
- R36 pad 2: /R -> Net-(R35-Pad2)
- R37 pad 1: Net-(IC5C-OUT) -> Net-(R35-Pad2)
- R37 pad 2: /B -> /Vector DACs/R2R_DAC_Y/D1
- R38 pad 1: Net-(R13-Pad2) -> Net-(R35-Pad2)
- R38 pad 2: Net-(R29-Pad1) -> Net-(R38-Pad2)
- R39 pad 1: Net-(R29-Pad1) -> Net-(R35-Pad2)
- R39 pad 2: Net-(R30-Pad1) -> Net-(R38-Pad2)
- R4 pad 1: Net-(R15-Pad1) -> Net-(R2-Pad2)
- R4 pad 2: Net-(R14-Pad1) -> /Vector DACs/R2R_DAC_B/D1
- R40 pad 1: Net-(R30-Pad1) -> Net-(R38-Pad2)
- R40 pad 2: Net-(R31-Pad1) -> /Vector DACs/R2R_DAC_Y/D0
- R44 pad 1: Net-(R32-Pad1) -> Net-(R38-Pad2)
- R44 pad 2: Net-(R33-Pad1) -> GND
- R45 pad 1: Net-(R33-Pad1) -> /JAMMA_P1_BUTTON4
- R45 pad 2: Net-(R34-Pad1) -> +5V
- R46 pad 1: Net-(IC5B--IN) -> /JAMMA_P1_BUTTON3
- R46 pad 2: Net-(IC5B-OUT) -> +5V
- R47 pad 1: Net-(IC5C--IN) -> /JAMMA_P1_BUTTON2
- R47 pad 2: Net-(IC5C-OUT) -> +5V
- R48 pad 1: Net-(R34-Pad1) -> /JAMMA_P1_BUTTON1
- R48 pad 2: Net-(R35-Pad1) -> +5V
- R49 pad 1: Net-(R35-Pad1) -> /JAMMA_P1_R
- R49 pad 2: Net-(R12-Pad1) -> +5V
- R5 pad 1: Net-(R16-Pad1) -> Net-(R2-Pad2)
- R5 pad 2: Net-(R15-Pad1) -> Net-(R5-Pad2)
- R50 pad 1: Net-(R12-Pad1) -> /JAMMA_P1_L
- R50 pad 2: GND -> +5V
- R54 pad 1: Net-(IC5A-OUT) -> /JAMMA_P1_COIN
- R54 pad 2: /G -> +5V
- R55 pad 1: Net-(IC5D-OUT) -> /JAMMA_TEST
- R55 pad 2: /+VREF -> +5V
- R56 pad 1: GND -> /Input P1/I11
- R56 pad 2: Net-(IC5A--IN) -> +5V
- R57 pad 1: GND -> +3.3V
- R57 pad 2: Net-(IC5D--IN) -> Net-(J7-Pad29)
- R58 pad 1: Net-(IC5D--IN) -> +5V
- R58 pad 2: Net-(IC5D-OUT) -> Net-(J7-Pad11)
- R59 pad 1: Net-(IC5A--IN) -> /JAMMA_P2_BUTTON4
- R59 pad 2: Net-(IC5A-OUT) -> +5V
- R6 pad 1: Net-(R17-Pad1) -> Net-(R2-Pad2)
- R6 pad 2: Net-(R16-Pad1) -> Net-(R5-Pad2)
- R64 pad 1: Net-(IC7C-OUT) -> Net-(U13B--IN)
- R64 pad 2: /VEC_X -> Net-(U13B-OUT)
- R65 pad 1: Net-(IC7B-OUT) -> Net-(U13C--IN)
- R65 pad 2: Net-(IC7C--IN) -> Net-(U13C-OUT)
- R68 pad 1: /+VREF -> Net-(U13D--IN)
- R68 pad 2: Net-(IC7B--IN) -> Net-(U13D-OUT)
- R69 pad 1: Net-(IC7B--IN) -> /Vector Amplifiers/+VREF
- R69 pad 2: Net-(IC7B-OUT) -> Net-(U13A--IN)
- R7 pad 1: Net-(R18-Pad1) -> Net-(R5-Pad2)
- R7 pad 2: Net-(R17-Pad1) -> /Vector DACs/R2R_DAC_B/D0
- R70 pad 1: Net-(IC7C--IN) -> Net-(U13A--IN)
- R70 pad 2: Net-(IC7C-OUT) -> Net-(U13A-OUT)
- R8 pad 1: Net-(R19-Pad1) -> Net-(R5-Pad2)
- R8 pad 2: Net-(R18-Pad1) -> GND
- R81 pad 1: Net-(IC7D-OUT) -> GND
- R81 pad 2: /VEC_Y -> Net-(U14D--IN)
- R82 pad 1: Net-(IC7A-OUT) -> Net-(U14D--IN)
- R82 pad 2: Net-(IC7D--IN) -> Net-(U14D-OUT)
- R87 pad 1: Net-(IC7D--IN) -> /JAMMA_P2_D
- R87 pad 2: Net-(IC7D-OUT) -> +5V
- R88 pad 1: /+VREF -> /JAMMA_P2_U
- R88 pad 2: Net-(IC7A--IN) -> +5V
- R89 pad 1: Net-(IC7A--IN) -> /JAMMA_P2_START
- R89 pad 2: Net-(IC7A-OUT) -> +5V
- R9 pad 1: Net-(R10-Pad2) -> /Vector Amplifiers/DAC_G
- R9 pad 2: Net-(R19-Pad1) -> /Vector DACs/R2R_DAC_G/D2
- R97 pad 1: /DAC_G -> /AUDIO_R
- R97 pad 2: /R2R_DAC_G/D2 -> Net-(C40-Pad2)
- R98 pad 1: Net-(R107-Pad2) -> /AUDIO_L
- R98 pad 2: /R2R_DAC_G/D1 -> Net-(C40-Pad2)
- R99 pad 1: Net-(R108-Pad2) -> Net-(U12--IN)
- R99 pad 2: /R2R_DAC_G/D0 -> Net-(R99-Pad2)
- U2 pad 1: GND -> /Vector DACs/R2R_DAC_X/D2
- U2 pad 10: /D8 -> unconnected-(U2-Pad10)
- U2 pad 11: /D9 -> unconnected-(U2-Pad11)
- U2 pad 12: GND -> unconnected-(U2-Pad12)
- U2 pad 13: /CLK_X -> unconnected-(U2-Pad13)
- U2 pad 14: /R2R_DAC_X/D9 -> unconnected-(U2-Pad14)
- U2 pad 15: /R2R_DAC_X/D8 -> unconnected-(U2-Pad15)
- U2 pad 16: /R2R_DAC_X/D7 -> Net-(R25-Pad1)
- U2 pad 2: /D0 -> /Vector DACs/R2R_DAC_X/D3
- U2 pad 3: /D1 -> /Vector DACs/R2R_DAC_X/D4
- U2 pad 4: /D2 -> /Vector DACs/R2R_DAC_X/D5
- U2 pad 5: /D3 -> /Vector DACs/R2R_DAC_X/D6
- U2 pad 6: /D4 -> /Vector DACs/R2R_DAC_X/D7
- U2 pad 7: /D5 -> /Vector DACs/R2R_DAC_X/D8
- U2 pad 8: /D6 -> /Vector DACs/R2R_DAC_X/D9
- U2 pad 9: /D7 -> /Vector Amplifiers/DAC_X
- U3 pad 1: GND -> /Vector DACs/R2R_DAC_Y/D2
- U3 pad 10: /D8 -> unconnected-(U3-Pad10)
- U3 pad 11: /D9 -> unconnected-(U3-Pad11)
- U3 pad 12: GND -> unconnected-(U3-Pad12)
- U3 pad 13: /CLK_Y -> unconnected-(U3-Pad13)
- U3 pad 14: /R2R_DAC_Y/D9 -> unconnected-(U3-Pad14)
- U3 pad 15: /R2R_DAC_Y/D8 -> unconnected-(U3-Pad15)
- U3 pad 16: /R2R_DAC_Y/D7 -> Net-(R35-Pad1)
- U3 pad 2: /D0 -> /Vector DACs/R2R_DAC_Y/D3
- U3 pad 3: /D1 -> /Vector DACs/R2R_DAC_Y/D4
- U3 pad 4: /D2 -> /Vector DACs/R2R_DAC_Y/D5
- U3 pad 5: /D3 -> /Vector DACs/R2R_DAC_Y/D6
- U3 pad 6: /D4 -> /Vector DACs/R2R_DAC_Y/D7
- U3 pad 7: /D5 -> /Vector DACs/R2R_DAC_Y/D8
- U3 pad 8: /D6 -> /Vector DACs/R2R_DAC_Y/D9
- U3 pad 9: /D7 -> /Vector Amplifiers/DAC_Y
- U4 pad 1: GND -> /D0
- U4 pad 10: /D8 -> /JAMMA_P1_L
- U4 pad 11: /D9 -> /JAMMA_P1_R
- U4 pad 12: GND -> /JAMMA_P1_BUTTON1
- U4 pad 13: /CLK_RGB -> /JAMMA_P1_BUTTON2
- U4 pad 14: unconnected-(U4-10Q-Pad14) -> /JAMMA_P1_BUTTON3
- U4 pad 15: /R2R_DAC_B/D2 -> +5V
- U4 pad 16: /R2R_DAC_B/D1 -> /JAMMA_P1_BUTTON4
- U4 pad 2: /D0 -> +3.3V
- U4 pad 8: /D6 -> /CLK_P10
- U4 pad 9: /D7 -> GND
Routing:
- net +5V: track 52.4 -> 407.8 mm, vias 0 -> 9
- net /JAMMA_SPEAKER+: track 0.00 -> 106.8 mm
- net /JAMMA_SPEAKER-: track 0.00 -> 98.3 mm, vias 0 -> 1
- net /Vector Amplifiers/DAC_B: track 0.00 -> 96.5 mm, vias 0 -> 2
- net /JAMMA_PIN_11(Y): track 0.00 -> 89.4 mm, vias 0 -> 2
- net /AUDIO_R: track 86.2 -> 3.05 mm, vias 1 -> 0
- net /Vector Amplifiers/DAC_G: track 0.00 -> 81.6 mm, vias 0 -> 2
- net /AUDIO_L: track 87.2 -> 6.59 mm, vias 1 -> 0
- net /JAMMA_PIN_M(X): track 0.00 -> 78.8 mm, vias 0 -> 2
- net GND: track 0.00 -> 77.2 mm, vias 0 -> 56
- net /Vector Amplifiers/DAC_R: track 0.00 -> 75.7 mm, vias 0 -> 2
- net /D0: track 59.6 -> 128.8 mm, vias 0 -> 7
- net /D2: track 62.2 -> 130.0 mm, vias 0 -> 6
- net /D1: track 60.9 -> 128.0 mm, vias 0 -> 6
- net /D5: track 68.5 -> 133.0 mm, vias 0 -> 6
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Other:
- board size 68.6 x 106.6 mm -> 114.8 x 118.8 mm
- board text added: "FAN 5V"
- board text added: "MISTER VECTOR JAMMA V1.0 ©2025"
- board text added: "VOLUME"
- board text removed: "0V to +5V"
- board text removed: "B"
- board text removed: "ElectronAsh Oct 2022"
- board text removed: "G"
- board text removed: "GND"
- board text removed: "MiSTer Vector + Dual VGA"
- board text removed: "X"
- board text removed: "Y"
